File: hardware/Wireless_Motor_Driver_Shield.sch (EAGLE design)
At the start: 96 parts, among them J1 5.5x2.1mm Barrel, Q1 MOSFET-NCHANNELBSS138, Q2 MOSFET-NCHANNELBSS138, Q3 MMBT2222A, Q4 DMG2307L, Q5 DMG2307L, Q6 DMG2307L, U1 XBEE-1XBEE-1_LOCK, U2 ARDUINO, U3 TB6612FNG

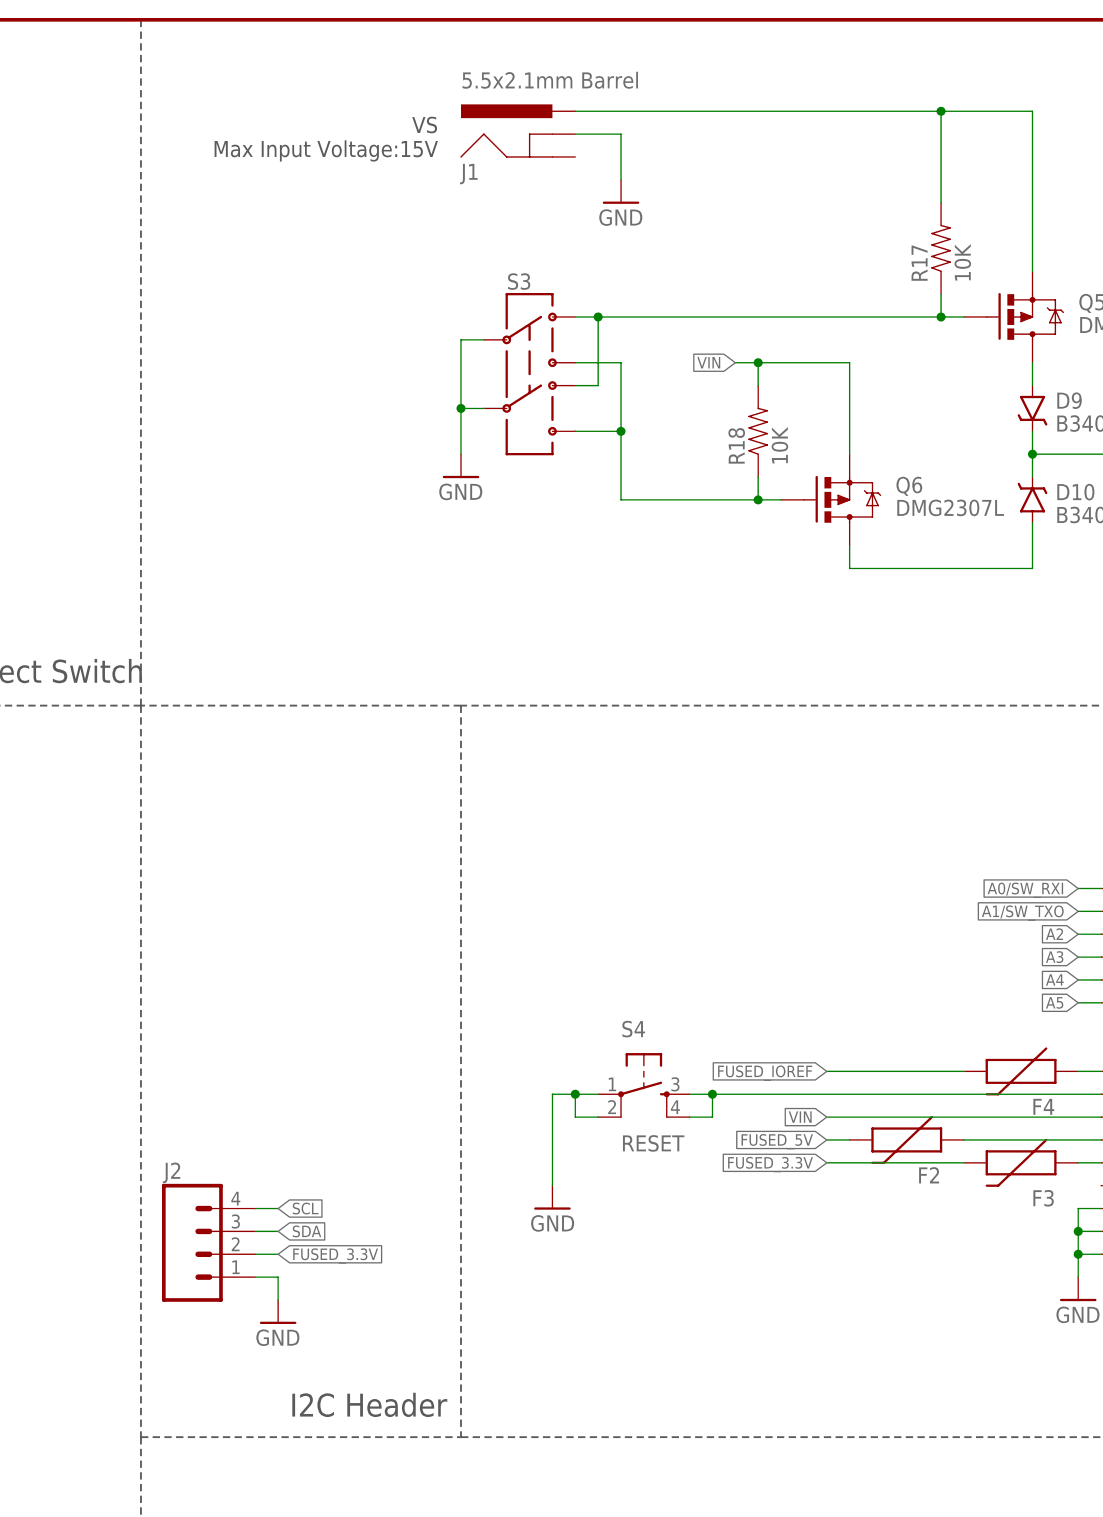
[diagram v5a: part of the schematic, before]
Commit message: Added staking vias to barrel jack. Added header PTH for VS.
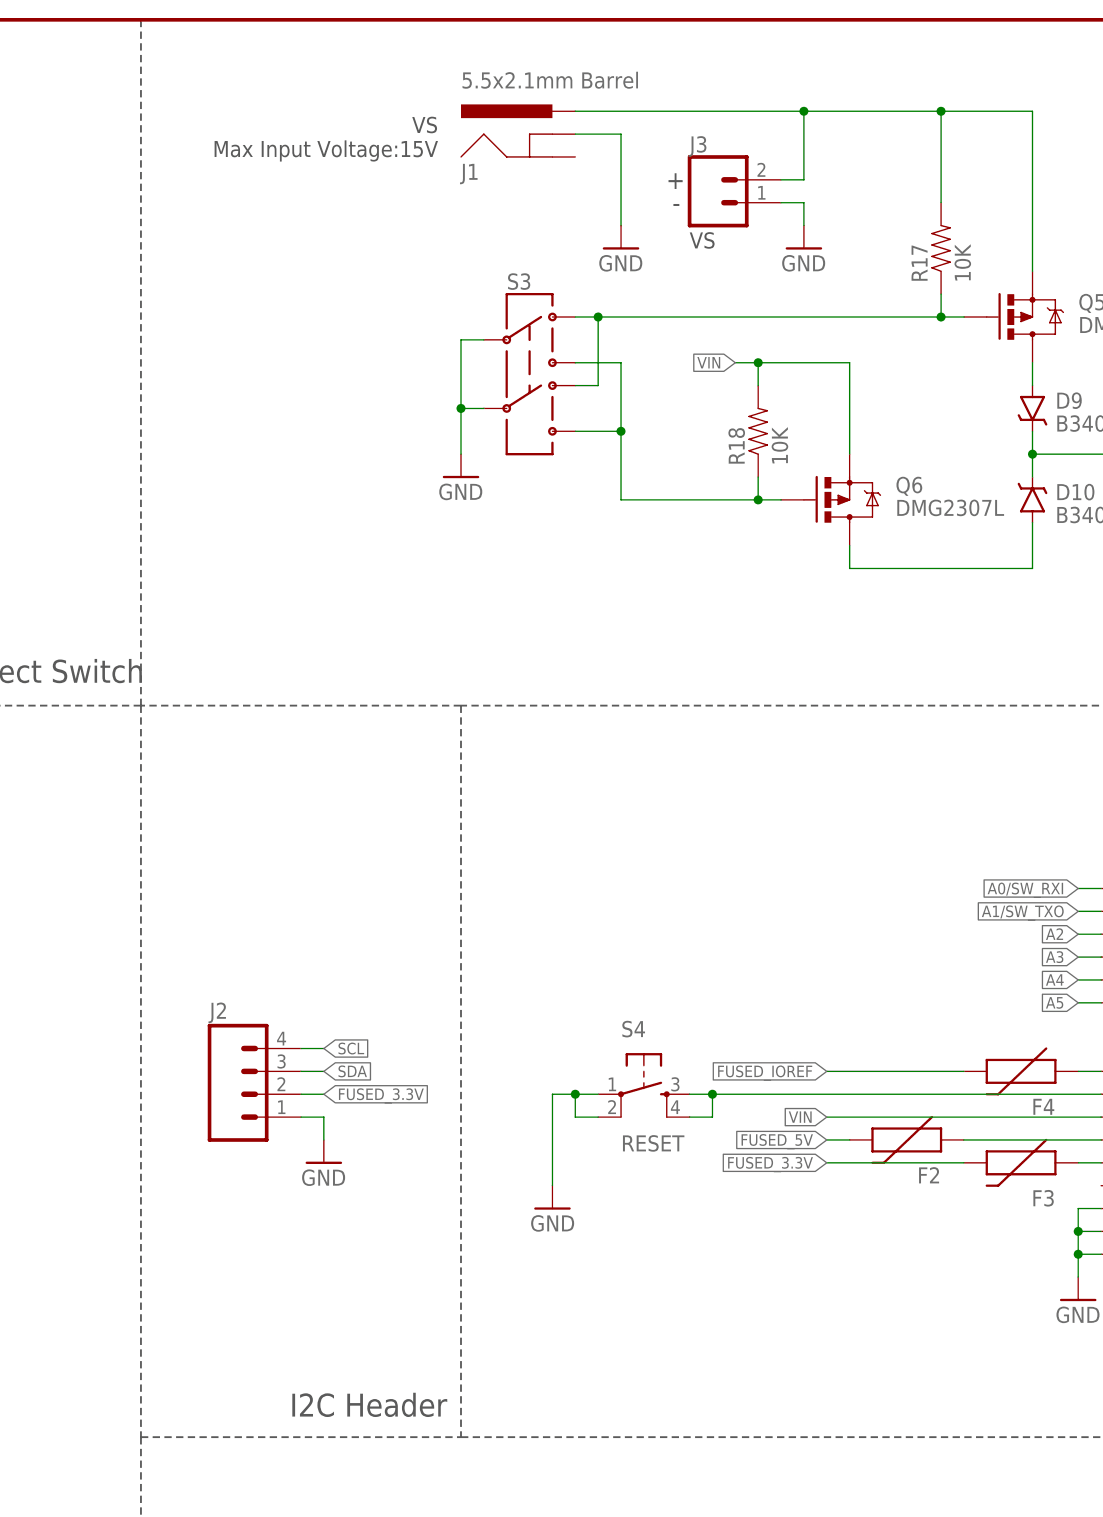
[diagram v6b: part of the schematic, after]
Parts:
- added J3: (no value), SparkFun-Connectors:CONN_021X02_NO_SILK
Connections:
- net GND: now also J3.1
- net N$10: now also J3.2
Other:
- note added: "+"
- note added: "-"
- note added: "VS"
- moved on the sheet: J2
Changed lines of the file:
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@@
 <setting verticaltext="up"/>
 </settings>
-<grid distance="0.1" unitdist="inch" unit="inch" style="lines" multiple="1" display="no" altdistance="0.01" altunitdist="inch" altunit="inch"/>
+<grid distance="0.1" unitdist="inch" unit="inch" style="lines" multiple="1" display="yes" altdistance="0.01" altunitdist="inch" altunit="inch"/>
 <layers>
 <layer number="1" name="Top" color="4" fill="1" visible="no" active="no"/>
@@
 <part name="GND20" library="SparkFun-Aesthetics" deviceset="GND" device=""/>
 <part name="C4" library="SparkFun-Capacitors" deviceset="10UF" device="-1210-50V-20%" value="10uF"/>
+<part name="J3" library="SparkFun-Connectors" deviceset="CONN_02" device="1X02_NO_SILK"/>
+<part name="GND21" library="SparkFun-Aesthetics" deviceset="GND" device=""/>
 </parts>
 <sheets>
@@
 <text x="292.1" y="264.16" size="1.778" layer="97" align="bottom-right">VS
 Max Input Voltage:15V</text>
+<text x="320.04" y="254" size="1.778" layer="97">VS</text>
+<text x="319.532" y="261.62" size="2.032" layer="97" align="center-right">+</text>
+<text x="319.024" y="259.08" size="2.032" layer="97" align="center-right">-</text>
 </plain>
 <instances>
@@
 <instance part="JP24" gate="G$1" x="71.12" y="162.56"/>
 <instance part="S1" gate="G$1" x="157.48" y="231.14"/>
-<instance part="GND8" gate="1" x="274.32" y="134.62"/>
+<instance part="GND8" gate="1" x="279.4" y="152.4"/>
 <instance part="GND9" gate="1" x="81.28" y="152.4"/>
 <instance part="GND10" gate="1" x="81.28" y="177.8"/>
@@
 <instance part="GND17" gate="1" x="149.86" y="22.86"/>
 <instance part="J1" gate="G$1" x="304.8" y="261.62"/>
-<instance part="GND18" gate="1" x="312.42" y="259.08"/>
+<instance part="GND18" gate="1" x="312.42" y="254"/>
 <instance part="S3" gate="G$1" x="302.26" y="241.3"/>
 <instance part="Q5" gate="G$1" x="358.14" y="246.38" smashed="yes" rot="MR180">
@@
 <attribute name="VALUE" x="360.68" y="223.4946" size="1.778" layer="96"/>
 </instance>
-<instance part="J2" gate="G$1" x="266.7" y="142.24"/>
+<instance part="J2" gate="G$1" x="271.78" y="160.02"/>
 <instance part="GND19" gate="1" x="294.64" y="228.6"/>
 <instance part="GND20" gate="1" x="373.38" y="215.9"/>
 <instance part="C4" gate="G$1" x="373.38" y="223.52"/>
+<instance part="J3" gate="G$1" x="322.58" y="259.08"/>
+<instance part="GND21" gate="1" x="332.74" y="254"/>
 </instances>
 <busses>
@@
 </segment>
 <segment>
-<wire x1="271.78" y1="139.7" x2="274.32" y2="139.7" width="0.1524" layer="91"/>
-<wire x1="274.32" y1="139.7" x2="274.32" y2="137.16" width="0.1524" layer="91"/>
+<wire x1="276.86" y1="157.48" x2="279.4" y2="157.48" width="0.1524" layer="91"/>
+<wire x1="279.4" y1="157.48" x2="279.4" y2="154.94" width="0.1524" layer="91"/>
 <pinref part="GND8" gate="1" pin="GND"/>
 <pinref part="J2" gate="G$1" pin="1"/>
@@
 <pinref part="J1" gate="G$1" pin="GNDBREAK"/>
 <wire x1="307.34" y1="266.7" x2="312.42" y2="266.7" width="0.1524" layer="91"/>
-<wire x1="312.42" y1="266.7" x2="312.42" y2="261.62" width="0.1524" layer="91"/>
+<wire x1="312.42" y1="266.7" x2="312.42" y2="256.54" width="0.1524" layer="91"/>
 <pinref part="GND18" gate="1" pin="GND"/>
 </segment>
@@
 <wire x1="373.38" y1="220.98" x2="373.38" y2="218.44" width="0.1524" layer="91"/>
 <pinref part="C4" gate="G$1" pin="2"/>
+</segment>
+<segment>
+<pinref part="J3" gate="G$1" pin="1"/>
+<wire x1="330.2" y1="259.08" x2="332.74" y2="259.08" width="0.1524" layer="91"/>
+<wire x1="332.74" y1="259.08" x2="332.74" y2="256.54" width="0.1524" layer="91"/>
+<pinref part="GND21" gate="1" pin="GND"/>
 </segment>
 </net>
@@
 </segment>
 <segment>
-<label x="274.32" y="144.78" size="1.27" layer="95" xref="yes"/>
-<wire x1="271.78" y1="144.78" x2="274.32" y2="144.78" width="0.1524" layer="91"/>
+<label x="279.4" y="162.56" size="1.27" layer="95" xref="yes"/>
+<wire x1="276.86" y1="162.56" x2="279.4" y2="162.56" width="0.1524" layer="91"/>
 <pinref part="J2" gate="G$1" pin="3"/>
 </segment>
@@
 </segment>
 <segment>
-<label x="274.32" y="147.32" size="1.27" layer="95" xref="yes"/>
-<wire x1="271.78" y1="147.32" x2="274.32" y2="147.32" width="0.1524" layer="91"/>
+<label x="279.4" y="165.1" size="1.27" layer="95" xref="yes"/>
+<wire x1="276.86" y1="165.1" x2="279.4" y2="165.1" width="0.1524" layer="91"/>
 <pinref part="J2" gate="G$1" pin="4"/>
 </segment>
@@
 </segment>
 <segment>
-<wire x1="271.78" y1="142.24" x2="274.32" y2="142.24" width="0.1524" layer="91"/>
-<label x="274.32" y="142.24" size="1.27" layer="95" xref="yes"/>
+<wire x1="276.86" y1="160.02" x2="279.4" y2="160.02" width="0.1524" layer="91"/>
+<label x="279.4" y="160.02" size="1.27" layer="95" xref="yes"/>
 <pinref part="J2" gate="G$1" pin="2"/>
 </segment>
@@
 <pinref part="J1" gate="G$1" pin="PWR"/>
 <pinref part="R17" gate="G$1" pin="2"/>
-<wire x1="307.34" y1="269.24" x2="347.98" y2="269.24" width="0.1524" layer="91"/>
+<wire x1="307.34" y1="269.24" x2="332.74" y2="269.24" width="0.1524" layer="91"/>
+<wire x1="332.74" y1="269.24" x2="347.98" y2="269.24" width="0.1524" layer="91"/>
 <wire x1="347.98" y1="269.24" x2="347.98" y2="259.08" width="0.1524" layer="91"/>
 <wire x1="347.98" y1="269.24" x2="358.14" y2="269.24" width="0.1524" layer="91"/>
@@
 <pinref part="Q5" gate="G$1" pin="S"/>
 <wire x1="358.14" y1="269.24" x2="358.14" y2="251.46" width="0.1524" layer="91"/>
-</segment>
-</net>
+<pinref part="J3" gate="G$1" pin="2"/>
+<wire x1="330.2" y1="261.62" x2="332.74" y2="261.62" width="0.1524" layer="91"/>
+<wire x1="332.74" y1="261.62" x2="332.74" y2="269.24" width="0.1524" layer="91"/>
+<junction x="332.74" y="269.24"/>
+</segment>
+</net>

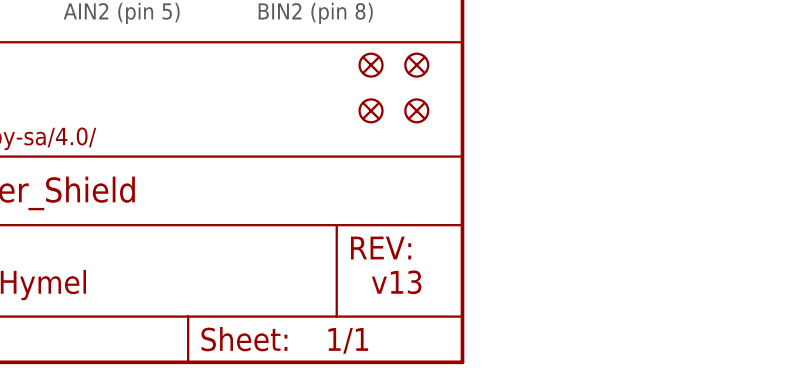
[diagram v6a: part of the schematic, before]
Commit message: Changed to v14. Changed switch labels to VMOTOR
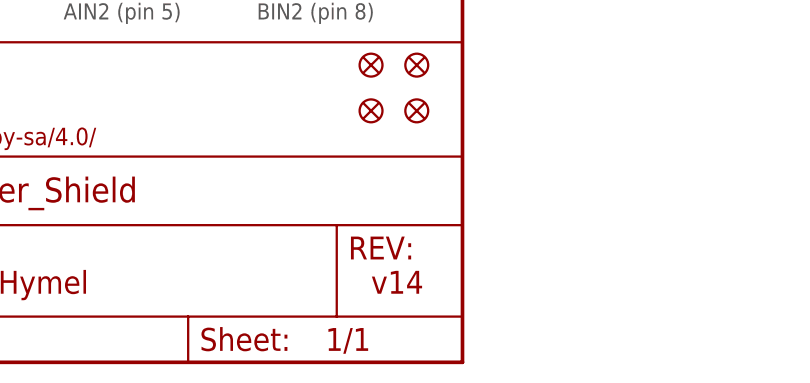
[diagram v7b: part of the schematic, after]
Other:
- note added: "v14"
- note removed: "v13"
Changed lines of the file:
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@@
 <setting verticaltext="up"/>
 </settings>
-<grid distance="0.1" unitdist="inch" unit="inch" style="lines" multiple="1" display="yes" altdistance="0.01" altunitdist="inch" altunit="inch"/>
+<grid distance="0.1" unitdist="inch" unit="inch" style="lines" multiple="1" display="no" altdistance="0.01" altunitdist="inch" altunit="inch"/>
 <layers>
 <layer number="1" name="Top" color="4" fill="1" visible="no" active="no"/>
@@
 <text x="350.52" y="7.62" size="2.54" layer="94">B. Huang
 Revised by Shawn Hymel</text>
-<text x="421.64" y="7.62" size="2.54" layer="94">v13</text>
+<text x="421.64" y="7.62" size="2.54" layer="94">v14</text>
 <wire x1="259.08" y1="121.92" x2="259.08" y2="0" width="0.2032" layer="97" style="longdash"/>
 <text x="275.59" y="124.206" size="2.54" layer="97">I2C Header</text>
